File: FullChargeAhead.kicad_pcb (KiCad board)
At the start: 2 copper layers, 18 parts, among them CON101 USB-MICRO-B, P101 CONN_01X02, P102 CONN_01X02, U101 MCP73834-FCI/UN

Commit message: Model update after component resze
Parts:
- added THERM1: 10K, Resistors_SMD:R_0805_HandSoldering, F.Cu at (130.6, 71.6)
- moved R102 7.73 mm to (142.2, 70.9)
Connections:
- net Net-(C101-Pad1) renamed /Vdd
- net Net-(C102-Pad1) renamed /Vbat
- U101 pad 8: Net-(R105-Pad2) -> Net-(THERM1-Pad2)

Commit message: Preperation for layout
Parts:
- P102: footprint Pin_Headers:Pin_Header_Straight_1x02 -> fca-lib:JST_2Pin
- THERM1: footprint Resistors_SMD:R_0805_HandSoldering -> Resistors_ThroughHole:Resistor_Vertical_RM5mm
- moved U101 10.2 mm to (142.2, 81.0)
- moved THERM1 6.55 mm to (126.7, 66.3)
- moved P102 3.69 mm to (138.9, 102.1), turned to 0 degrees
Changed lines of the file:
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@@
       (effects (font (size 1 1) (thickness 0.15)))
     )
-    (fp_text value 4.7uF (at 0 2.3) (layer F.Fab)
+    (fp_text value 4.7uF (at 0 2.3) (layer F.Fab) hide
       (effects (font (size 1 1) (thickness 0.15)))
     )
@@
       (effects (font (size 1 1) (thickness 0.15)))
     )
-    (fp_text value 4.7uF (at 0 2.3) (layer F.Fab)
+    (fp_text value 4.7uF (at 0 2.3) (layer F.Fab) hide
       (effects (font (size 1 1) (thickness 0.15)))
     )
@@
       (effects (font (size 1.5 1.5) (thickness 0.15)))
     )
-    (fp_text value USB-MICRO-B (at 0 3.2 270) (layer F.Fab)
+    (fp_text value USB-MICRO-B (at 0 3.2 270) (layer F.Fab) hide
       (effects (font (size 1.5 1.5) (thickness 0.15)))
     )
@@
       (effects (font (size 1 1) (thickness 0.15)))
     )
-    (fp_text value LED (at 0 1.27) (layer F.Fab)
+    (fp_text value LED (at 0 1.27) (layer F.Fab) hide
       (effects (font (size 1 1) (thickness 0.15)))
     )
@@
       (effects (font (size 1 1) (thickness 0.15)))
     )
-    (fp_text value CONN_01X02 (at 0 -3.1 90) (layer F.Fab)
+    (fp_text value CONN_01X02 (at 0 -3.1 90) (layer F.Fab) hide
       (effects (font (size 1 1) (thickness 0.15)))
     )
@@
     )
   )
-  (module Pin_Headers:Pin_Header_Straight_1x02 (layer F.Cu)
-    (at 135.8392 100.1014 90)
-    (descr "Through hole pin header")
-    (tags "pin header")
-    (fp_text reference P102 (at 0 -5.1 90) (layer F.SilkS)
-      (effects (font (size 1 1) (thickness 0.15)))
-    )
-    (fp_text value CONN_01X02 (at 0 -3.1 90) (layer F.Fab)
-      (effects (font (size 1 1) (thickness 0.15)))
-    )
-    (fp_line (start 1.27 1.27) (end 1.27 3.81) (layer F.SilkS) (width 0.15))
-    (fp_line (start 1.55 -1.55) (end 1.55 0) (layer F.SilkS) (width 0.15))
-    (fp_line (start -1.75 -1.75) (end -1.75 4.3) (layer F.CrtYd) (width 0.05))
-    (fp_line (start 1.75 -1.75) (end 1.75 4.3) (layer F.CrtYd) (width 0.05))
-    (fp_line (start -1.75 -1.75) (end 1.75 -1.75) (layer F.CrtYd) (width 0.05))
-    (fp_line (start -1.75 4.3) (end 1.75 4.3) (layer F.CrtYd) (width 0.05))
-    (fp_line (start 1.27 1.27) (end -1.27 1.27) (layer F.SilkS) (width 0.15))
-    (fp_line (start -1.55 0) (end -1.55 -1.55) (layer F.SilkS) (width 0.15))
-    (fp_line (start -1.55 -1.55) (end 1.55 -1.55) (layer F.SilkS) (width 0.15))
-    (fp_line (start -1.27 1.27) (end -1.27 3.81) (layer F.SilkS) (width 0.15))
-    (fp_line (start -1.27 3.81) (end 1.27 3.81) (layer F.SilkS) (width 0.15))
-    (pad 1 thru_hole rect (at 0 0 90) (size 2.032 2.032) (drill 1.016) (layers *.Cu *.Mask F.SilkS)
-      (net 15 /Vbat))
-    (pad 2 thru_hole oval (at 0 2.54 90) (size 2.032 2.032) (drill 1.016) (layers *.Cu *.Mask F.SilkS)
-      (net 1 GND))
-    (model Pin_Headers.3dshapes/Pin_Header_Straight_1x02.wrl
-      (at (xyz 0 -0.05 0))
-      (scale (xyz 1 1 1))
-      (rotate (xyz 0 0 90))
-    )
-  )
   (module Resistors_SMD:R_0805_HandSoldering (layer F.Cu)
     (at 158.0642 74.8538)
@@
       (effects (font (size 1 1) (thickness 0.15)))
     )
-    (fp_text value 470 (at 0 2.1) (layer F.Fab)
+    (fp_text value 470 (at 0 2.1) (layer F.Fab) hide
       (effects (font (size 1 1) (thickness 0.15)))
     )
@@
       (effects (font (size 1 1) (thickness 0.15)))
     )
-    (fp_text value 470 (at 0 2.1) (layer F.Fab)
+    (fp_text value 470 (at 0 2.1) (layer F.Fab) hide
       (effects (font (size 1 1) (thickness 0.15)))
     )
@@
       (effects (font (size 1 1) (thickness 0.15)))
     )
-    (fp_text value NOPOP (at 0 2.1) (layer F.Fab)
+    (fp_text value NOPOP (at 0 2.1) (layer F.Fab) hide
       (effects (font (size 1 1) (thickness 0.15)))
     )
@@
       (effects (font (size 1 1) (thickness 0.15)))
     )
-    (fp_text value 1K (at 0 2.1 180) (layer F.Fab)
+    (fp_text value 1K (at 0 2.1 180) (layer F.Fab) hide
       (effects (font (size 1 1) (thickness 0.15)))
     )
@@
       (effects (font (size 1 1) (thickness 0.15)))
     )
-    (fp_text value 10K (at 0 2.1) (layer F.Fab)
+    (fp_text value 10K (at 0 2.1) (layer F.Fab) hide
       (effects (font (size 1 1) (thickness 0.15)))
     )
@@
       (effects (font (size 1 1) (thickness 0.15)))
     )
-    (fp_text value NOPOP (at 0 2.1) (layer F.Fab)
+    (fp_text value NOPOP (at 0 2.1) (layer F.Fab) hide
       (effects (font (size 1 1) (thickness 0.15)))
     )
@@
       (effects (font (size 1 1) (thickness 0.15)))
     )
-    (fp_text value NOPOP (at 0 2.1) (layer F.Fab)
+    (fp_text value NOPOP (at 0 2.1) (layer F.Fab) hide
       (effects (font (size 1 1) (thickness 0.15)))
     )
@@
   )
   (module Housings_SSOP:MSOP-10_3x3mm_Pitch0.5mm (layer F.Cu)
-    (at 132.207 82.9564)
+    (at 142.24 81.026)
     (descr "10-Lead Plastic Micro Small Outline Package (MS) [MSOP] (see Microchip Packaging Specification 00000049BS.pdf)")
     (tags "SSOP 0.5")
@@
       (effects (font (size 1 1) (thickness 0.15)))
     )
-    (fp_text value MCP73834-FCI/UN (at 0 2.6) (layer F.Fab)
+    (fp_text value MCP73834-FCI/UN (at 0 2.6) (layer F.Fab) hide
       (effects (font (size 1 1) (thickness 0.15)))
     )
@@
     )
   )
-  (module Resistors_SMD:R_0805_HandSoldering (layer F.Cu)
-    (at 130.556 71.628)
-    (descr "Resistor SMD 0805, hand soldering")
-    (tags "resistor 0805")
-    (attr smd)
-    (fp_text reference THERM1 (at 0 -2.1) (layer F.SilkS)
-      (effects (font (size 1 1) (thickness 0.15)))
-    )
-    (fp_text value 10K (at 0 2.1) (layer F.Fab)
-      (effects (font (size 1 1) (thickness 0.15)))
-    )
-    (fp_line (start -2.4 -1) (end 2.4 -1) (layer F.CrtYd) (width 0.05))
-    (fp_line (start -2.4 1) (end 2.4 1) (layer F.CrtYd) (width 0.05))
-    (fp_line (start -2.4 -1) (end -2.4 1) (layer F.CrtYd) (width 0.05))
-    (fp_line (start 2.4 -1) (end 2.4 1) (layer F.CrtYd) (width 0.05))
-    (fp_line (start 0.6 0.875) (end -0.6 0.875) (layer F.SilkS) (width 0.15))
-    (fp_line (start -0.6 -0.875) (end 0.6 -0.875) (layer F.SilkS) (width 0.15))
-    (pad 1 smd rect (at -1.35 0) (size 1.5 1.3) (layers F.Cu F.Paste F.Mask)
-      (net 1 GND))
-    (pad 2 smd rect (at 1.35 0) (size 1.5 1.3) (layers F.Cu F.Paste F.Mask)
+  (module fca-lib:JST_2Pin (layer F.Cu)
+    (at 138.938 102.108)
+    (descr "Through hole pin header")
+    (tags "pin header")
+    (fp_text reference P102 (at 0.4 -2.8) (layer F.SilkS)
+      (effects (font (size 1 1) (thickness 0.15)))
+    )
+    (fp_text value CONN_01X02 (at 1.5748 5.334) (layer F.Fab) hide
+      (effects (font (size 1 1) (thickness 0.15)))
+    )
+    (fp_line (start -1.6 -1.9) (end -1.6 3.9) (layer F.SilkS) (width 0.127))
+    (fp_line (start 0 -1.9) (end -1.6 -1.9) (layer F.SilkS) (width 0.127))
+    (fp_line (start -1.6 3.9) (end 0 3.9) (layer F.SilkS) (width 0.127))
+    (fp_line (start 1.2 2) (end 6.8 2) (layer Eco1.User) (width 0.127))
+    (fp_line (start 1.2 0) (end 6.8 0) (layer Eco1.User) (width 0.127))
+    (fp_line (start 7.85 -1.95) (end 7.85 3.95) (layer Eco1.User) (width 0.15))
+    (fp_line (start -1.6 3.95) (end 7.85 3.95) (layer Eco1.User) (width 0.15))
+    (fp_line (start -1.6 -1.95) (end -1.6 3.95) (layer Eco1.User) (width 0.15))
+    (fp_line (start -1.6 -1.95) (end 7.85 -1.95) (layer Eco1.User) (width 0.15))
+    (pad 1 thru_hole circle (at 0 0) (size 1.5 1.5) (drill 0.7) (layers *.Cu *.Mask F.SilkS)
+      (net 15 /Vbat))
+    (pad 2 thru_hole circle (at 0 2) (size 1.5 1.5) (drill 0.7) (layers *.Cu *.Mask F.SilkS)
+      (net 1 GND))
+    (model Pin_Headers.3dshapes/Pin_Header_Angled_1x02.wrl
+      (at (xyz 0 -0.05 0))
+      (scale (xyz 1 1 1))
+      (rotate (xyz 0 0 90))
+    )
+  )
+  (module Resistors_ThroughHole:Resistor_Vertical_RM5mm (layer F.Cu)
+    (at 126.746 66.294)
+    (descr "Resistor, Vertical, RM 5mm, 1/3W,")
+    (tags "Resistor, Vertical, RM 5mm, 1/3W,")
+    (fp_text reference THERM1 (at 2.70002 -3.29946) (layer F.SilkS)
+      (effects (font (size 1 1) (thickness 0.15)))
+    )
+    (fp_text value 10K (at 0 4.50088) (layer F.Fab) hide
+      (effects (font (size 1 1) (thickness 0.15)))
+    )
+    (fp_line (start -0.09906 0) (end 0.9017 0) (layer F.SilkS) (width 0.15))
+    (fp_circle (center -2.49936 0) (end 0 0) (layer F.SilkS) (width 0.15))
+    (pad 1 thru_hole circle (at -2.49936 0) (size 1.99898 1.99898) (drill 1.00076) (layers *.Cu *.SilkS *.Mask)
+      (net 1 GND))
+    (pad 2 thru_hole circle (at 2.5019 0) (size 1.99898 1.99898) (drill 1.00076) (layers *.Cu *.SilkS *.Mask)
       (net 16 "Net-(THERM1-Pad2)"))
-    (model Resistors_SMD.3dshapes/R_0805_HandSoldering.wrl
-      (at (xyz 0 0 0))
-      (scale (xyz 1 1 1))
-      (rotate (xyz 0 0 0))
-    )
   )
 )

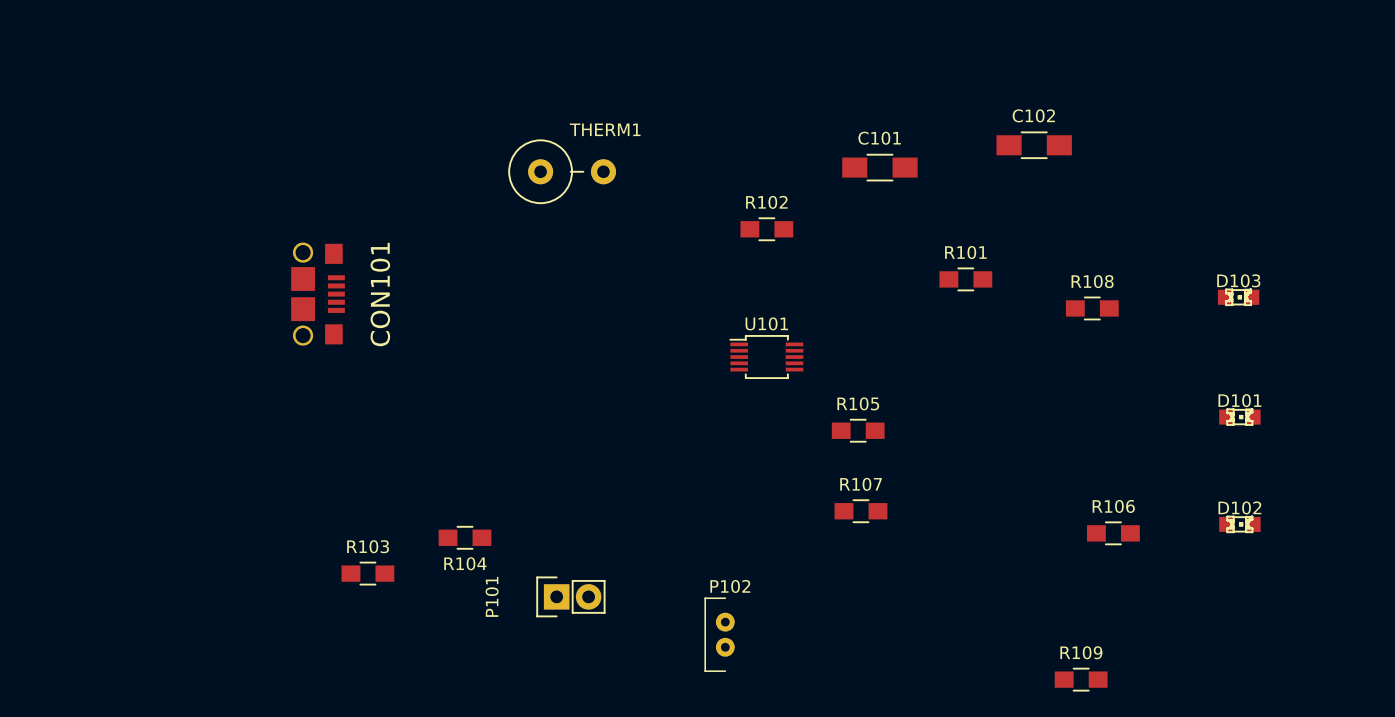
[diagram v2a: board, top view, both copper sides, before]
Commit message: Corrected the footprint for the JST connector
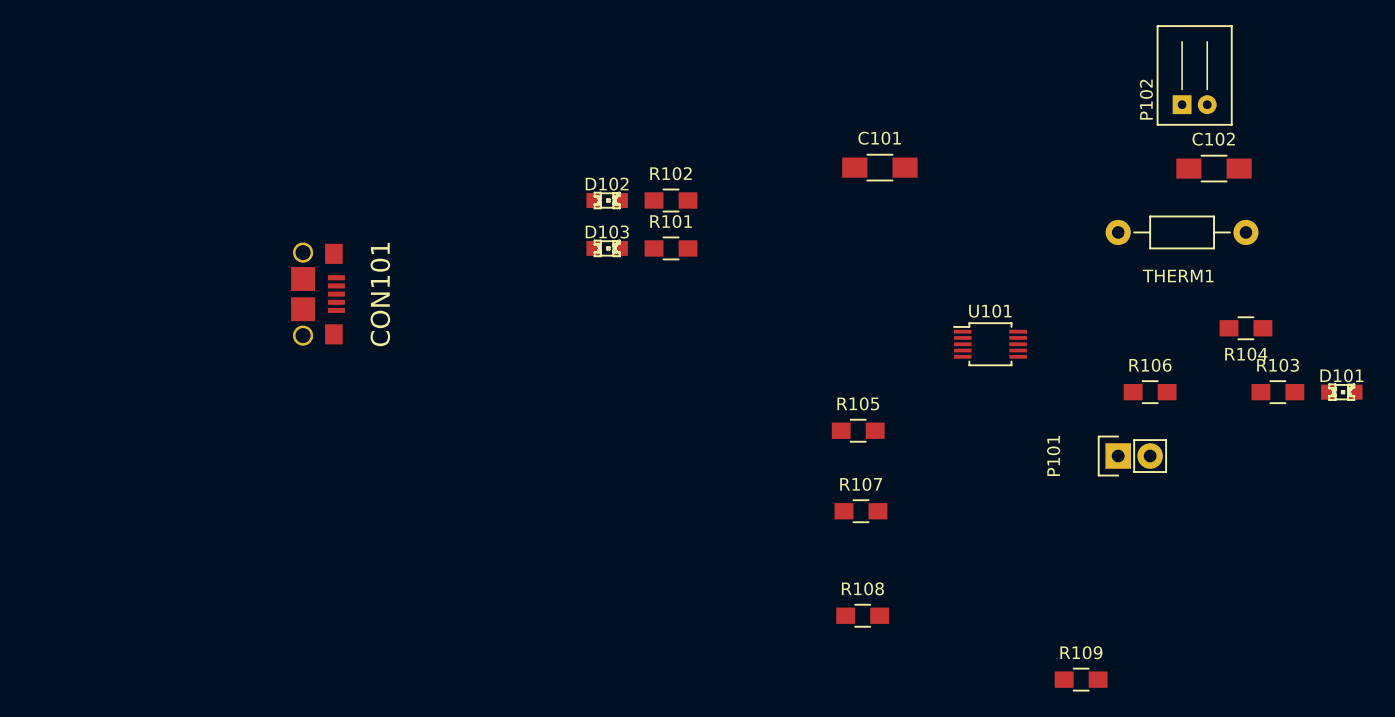
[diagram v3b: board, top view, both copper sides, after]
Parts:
- P102: value CONN_01X02 -> JST 2 Pin
- THERM1: footprint Resistors_ThroughHole:Resistor_Vertical_RM5mm -> Resistors_ThroughHole:Resistor_Horizontal_RM10mm
- moved R103 73.8 mm to (182.9, 83.8)
- moved R104 64.3 mm to (180.3, 78.7)
- moved D102 56.5 mm to (129.5, 68.6)
- moved P102 54.9 mm to (175.3, 61.0), turned to 90 degrees
- moved D103 50.4 mm to (129.5, 72.4)
- moved THERM1 48.8 mm to (175.3, 71.1), turned to 180 degrees
- moved P101 46.0 mm to (170.2, 88.9)
- moved R108 30.5 mm to (149.9, 101.6)
- moved R101 23.6 mm to (134.6, 72.4)
- moved U101 17.8 mm to (160.0, 80.0)
- moved C102 14.4 mm to (177.8, 66.0)
- moved R106 11.6 mm to (172.7, 83.8)
- moved D101 8.34 mm to (188.0, 83.8)
- moved R102 7.96 mm to (134.6, 68.6)
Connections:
- R107 pad 2: GND -> /Vdd
- R108 pad 2: GND -> /Vdd
- R109 pad 2: GND -> /Vdd
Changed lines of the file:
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@@
     (links 39)
     (no_connects 39)
-    (area 0 0 0 0)
+    (area 93.473057 60.7068 182.757829 109.809)
     (thickness 1.6)
     (drawings 0)
@@
     (pad_to_mask_clearance 0)
     (aux_axis_origin 0 0)
-    (visible_elements FFFFFF7F)
+    (visible_elements FFFFF77F)
     (pcbplotparams
       (layerselection 0x00030_80000001)
@@
   )
   (module Capacitors_SMD:C_1206_HandSoldering (layer F.Cu)
-    (at 163.4998 64.1858)
+    (at 177.8 66.04)
     (descr "Capacitor SMD 1206, hand soldering")
     (tags "capacitor 1206")
@@
   )
   (module LEDs:LED-0805 (layer F.Cu)
-    (at 179.8574 85.8012)
+    (at 187.96 83.82)
     (descr "LED 0805 smd package")
     (tags "LED 0805 SMD")
@@
   )
   (module LEDs:LED-0805 (layer F.Cu)
-    (at 179.8574 94.3356)
+    (at 129.54 68.58)
     (descr "LED 0805 smd package")
     (tags "LED 0805 SMD")
@@
   )
   (module LEDs:LED-0805 (layer F.Cu)
-    (at 179.7558 76.2762)
+    (at 129.54 72.39)
     (descr "LED 0805 smd package")
     (tags "LED 0805 SMD")
@@
   )
   (module Pin_Headers:Pin_Header_Straight_1x02 (layer F.Cu)
-    (at 125.5268 100.1014 90)
+    (at 170.18 88.9 90)
     (descr "Through hole pin header")
     (tags "pin header")
@@
   )
   (module Resistors_SMD:R_0805_HandSoldering (layer F.Cu)
-    (at 158.0642 74.8538)
+    (at 134.62 72.39)
     (descr "Resistor SMD 0805, hand soldering")
     (tags "resistor 0805")
@@
   )
   (module Resistors_SMD:R_0805_HandSoldering (layer F.Cu)
-    (at 142.24 70.866)
+    (at 134.62 68.58)
     (descr "Resistor SMD 0805, hand soldering")
     (tags "resistor 0805")
@@
   )
   (module Resistors_SMD:R_0805_HandSoldering (layer F.Cu)
-    (at 110.5154 98.2472)
+    (at 182.88 83.82)
     (descr "Resistor SMD 0805, hand soldering")
     (tags "resistor 0805")
@@
   )
   (module Resistors_SMD:R_0805_HandSoldering (layer F.Cu)
-    (at 118.237 95.4024 180)
+    (at 180.34 78.74 180)
     (descr "Resistor SMD 0805, hand soldering")
     (tags "resistor 0805")
@@
   )
   (module Resistors_SMD:R_0805_HandSoldering (layer F.Cu)
-    (at 169.799 95.0468)
+    (at 172.72 83.82)
     (descr "Resistor SMD 0805, hand soldering")
     (tags "resistor 0805")
@@
       (net 2 "Net-(CON101-Pad4)"))
     (pad 2 smd rect (at 1.35 0) (size 1.5 1.3) (layers F.Cu F.Paste F.Mask)
-      (net 1 GND))
-    (model Resistors_SMD.3dshapes/R_0805_HandSoldering.wrl
-      (at (xyz 0 0 0))
-      (scale (xyz 1 1 1))
-      (rotate (xyz 0 0 0))
-    )
-  )
-  (module Resistors_SMD:R_0805_HandSoldering (layer F.Cu)
-    (at 168.1226 77.1652)
+      (net 14 /Vdd))
+    (model Resistors_SMD.3dshapes/R_0805_HandSoldering.wrl
+      (at (xyz 0 0 0))
+      (scale (xyz 1 1 1))
+      (rotate (xyz 0 0 0))
+    )
+  )
+  (module Resistors_SMD:R_0805_HandSoldering (layer F.Cu)
+    (at 149.86 101.6)
     (descr "Resistor SMD 0805, hand soldering")
     (tags "resistor 0805")
@@
       (net 3 "Net-(CON101-Pad3)"))
     (pad 2 smd rect (at 1.35 0) (size 1.5 1.3) (layers F.Cu F.Paste F.Mask)
-      (net 1 GND))
+      (net 14 /Vdd))
     (model Resistors_SMD.3dshapes/R_0805_HandSoldering.wrl
       (at (xyz 0 0 0))
@@
       (net 4 "Net-(CON101-Pad2)"))
     (pad 2 smd rect (at 1.35 0) (size 1.5 1.3) (layers F.Cu F.Paste F.Mask)
-      (net 1 GND))
+      (net 14 /Vdd))
     (model Resistors_SMD.3dshapes/R_0805_HandSoldering.wrl
       (at (xyz 0 0 0))
@@
   )
   (module Housings_SSOP:MSOP-10_3x3mm_Pitch0.5mm (layer F.Cu)
-    (at 142.24 81.026)
+    (at 160.02 80.01)
     (descr "10-Lead Plastic Micro Small Outline Package (MS) [MSOP] (see Microchip Packaging Specification 00000049BS.pdf)")
     (tags "SSOP 0.5")
@@
   )
   (module fca-lib:JST_2Pin (layer F.Cu)
-    (at 138.938 102.108)
+    (at 175.26 60.96 90)
     (descr "Through hole pin header")
     (tags "pin header")
-    (fp_text reference P102 (at 0.4 -2.8) (layer F.SilkS)
-      (effects (font (size 1 1) (thickness 0.15)))
-    )
-    (fp_text value CONN_01X02 (at 1.5748 5.334) (layer F.Fab) hide
-      (effects (font (size 1 1) (thickness 0.15)))
-    )
-    (fp_line (start -1.6 -1.9) (end -1.6 3.9) (layer F.SilkS) (width 0.127))
-    (fp_line (start 0 -1.9) (end -1.6 -1.9) (layer F.SilkS) (width 0.127))
-    (fp_line (start -1.6 3.9) (end 0 3.9) (layer F.SilkS) (width 0.127))
-    (fp_line (start 1.2 2) (end 6.8 2) (layer Eco1.User) (width 0.127))
-    (fp_line (start 1.2 0) (end 6.8 0) (layer Eco1.User) (width 0.127))
-    (fp_line (start 7.85 -1.95) (end 7.85 3.95) (layer Eco1.User) (width 0.15))
-    (fp_line (start -1.6 3.95) (end 7.85 3.95) (layer Eco1.User) (width 0.15))
-    (fp_line (start -1.6 -1.95) (end -1.6 3.95) (layer Eco1.User) (width 0.15))
-    (fp_line (start -1.6 -1.95) (end 7.85 -1.95) (layer Eco1.User) (width 0.15))
-    (pad 1 thru_hole circle (at 0 0) (size 1.5 1.5) (drill 0.7) (layers *.Cu *.Mask F.SilkS)
+    (fp_text reference P102 (at 0.4 -2.8 90) (layer F.SilkS)
+      (effects (font (size 1 1) (thickness 0.15)))
+    )
+    (fp_text value "JST 2 Pin" (at 1.5748 5.334 90) (layer F.Fab) hide
+      (effects (font (size 1 1) (thickness 0.15)))
+    )
+    (fp_line (start 1.2 2) (end 5 2) (layer F.SilkS) (width 0.127))
+    (fp_line (start 1.2 0) (end 5 0) (layer F.SilkS) (width 0.127))
+    (fp_line (start 6.25 -1.95) (end 6.25 3.95) (layer F.SilkS) (width 0.15))
+    (fp_line (start -1.6 3.95) (end 6.25 3.95) (layer F.SilkS) (width 0.15))
+    (fp_line (start -1.6 -1.95) (end -1.6 3.95) (layer F.SilkS) (width 0.15))
+    (fp_line (start -1.6 -1.95) (end 6.25 -1.95) (layer F.SilkS) (width 0.15))
+    (pad 1 thru_hole rect (at 0 0 90) (size 1.5 1.5) (drill 0.7) (layers *.Cu *.Mask F.SilkS)
       (net 15 /Vbat))
-    (pad 2 thru_hole circle (at 0 2) (size 1.5 1.5) (drill 0.7) (layers *.Cu *.Mask F.SilkS)
+    (pad 2 thru_hole circle (at 0 2 90) (size 1.5 1.5) (drill 0.7) (layers *.Cu *.Mask F.SilkS)
       (net 1 GND))
     (model Pin_Headers.3dshapes/Pin_Header_Angled_1x02.wrl
@@
     )
   )
-  (module Resistors_ThroughHole:Resistor_Vertical_RM5mm (layer F.Cu)
-    (at 126.746 66.294)
-    (descr "Resistor, Vertical, RM 5mm, 1/3W,")
-    (tags "Resistor, Vertical, RM 5mm, 1/3W,")
-    (fp_text reference THERM1 (at 2.70002 -3.29946) (layer F.SilkS)
-      (effects (font (size 1 1) (thickness 0.15)))
-    )
-    (fp_text value 10K (at 0 4.50088) (layer F.Fab) hide
-      (effects (font (size 1 1) (thickness 0.15)))
-    )
-    (fp_line (start -0.09906 0) (end 0.9017 0) (layer F.SilkS) (width 0.15))
-    (fp_circle (center -2.49936 0) (end 0 0) (layer F.SilkS) (width 0.15))
-    (pad 1 thru_hole circle (at -2.49936 0) (size 1.99898 1.99898) (drill 1.00076) (layers *.Cu *.SilkS *.Mask)
-      (net 1 GND))
-    (pad 2 thru_hole circle (at 2.5019 0) (size 1.99898 1.99898) (drill 1.00076) (layers *.Cu *.SilkS *.Mask)
+  (module Resistors_ThroughHole:Resistor_Horizontal_RM10mm (layer F.Cu)
+    (at 175.26 71.12 180)
+    (descr "Resistor, Axial,  RM 10mm, 1/3W,")
+    (tags "Resistor, Axial, RM 10mm, 1/3W,")
+    (fp_text reference THERM1 (at 0.24892 -3.50012 180) (layer F.SilkS)
+      (effects (font (size 1 1) (thickness 0.15)))
+    )
+    (fp_text value 10K (at 3.81 3.81 180) (layer F.Fab)
+      (effects (font (size 1 1) (thickness 0.15)))
+    )
+    (fp_line (start -2.54 -1.27) (end 2.54 -1.27) (layer F.SilkS) (width 0.15))
+    (fp_line (start 2.54 -1.27) (end 2.54 1.27) (layer F.SilkS) (width 0.15))
+    (fp_line (start 2.54 1.27) (end -2.54 1.27) (layer F.SilkS) (width 0.15))
+    (fp_line (start -2.54 1.27) (end -2.54 -1.27) (layer F.SilkS) (width 0.15))
+    (fp_line (start -2.54 0) (end -3.81 0) (layer F.SilkS) (width 0.15))
+    (fp_line (start 2.54 0) (end 3.81 0) (layer F.SilkS) (width 0.15))
+    (pad 1 thru_hole circle (at -5.08 0 180) (size 1.99898 1.99898) (drill 1.00076) (layers *.Cu *.SilkS *.Mask)
+      (net 1 GND))
+    (pad 2 thru_hole circle (at 5.08 0 180) (size 1.99898 1.99898) (drill 1.00076) (layers *.Cu *.SilkS *.Mask)
       (net 16 "Net-(THERM1-Pad2)"))
+    (model Resistors_ThroughHole.3dshapes/Resistor_Horizontal_RM10mm.wrl
+      (at (xyz 0 0 0))
+      (scale (xyz 0.4 0.4 0.4))
+      (rotate (xyz 0 0 0))
+    )
   )
 )
